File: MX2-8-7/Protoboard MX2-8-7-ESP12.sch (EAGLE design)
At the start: 140 parts, among them J1 DCJ0202

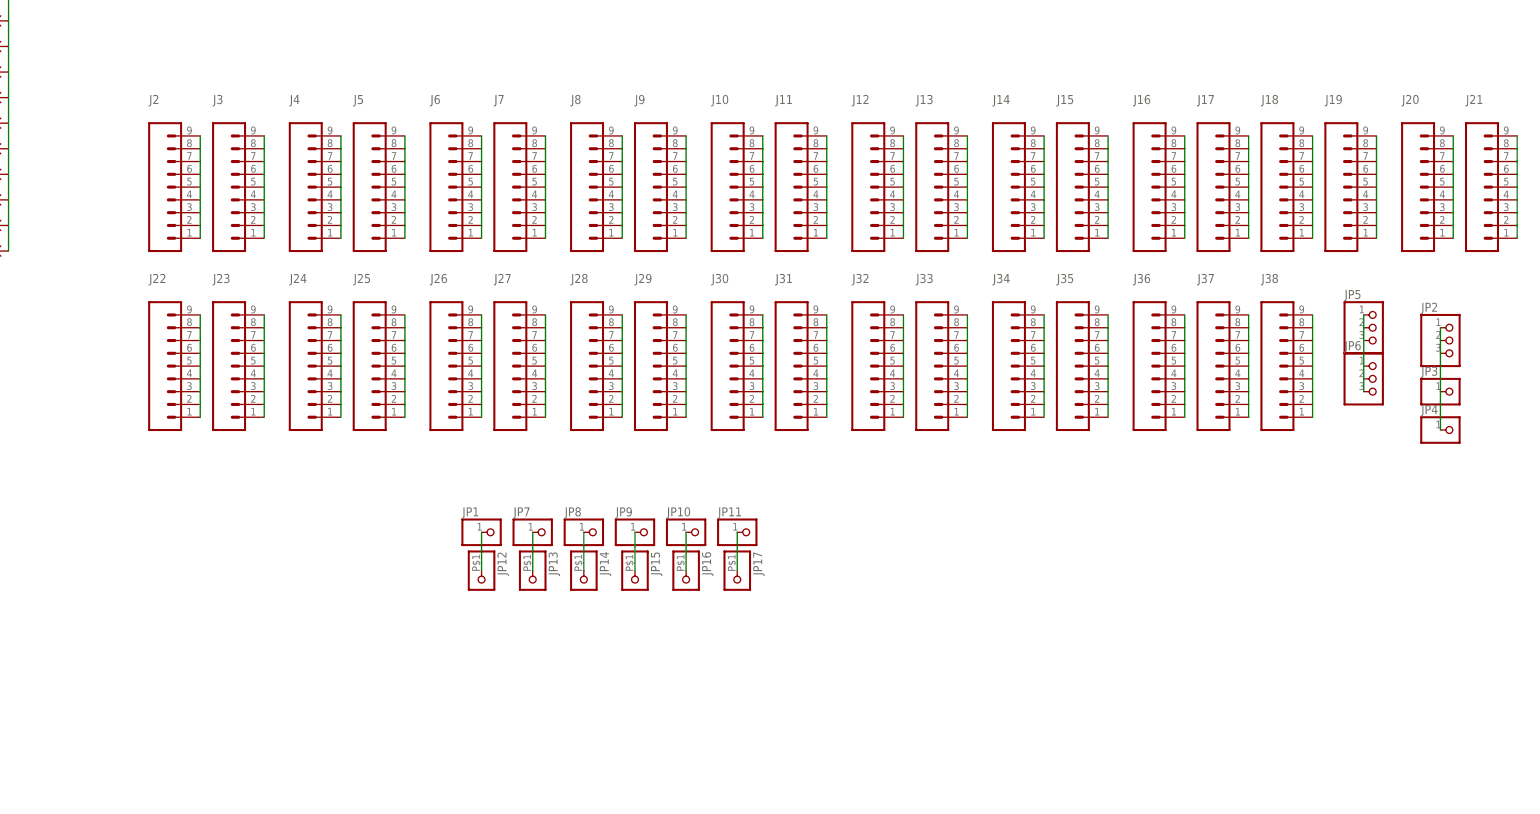
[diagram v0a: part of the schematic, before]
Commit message: Update to rev2
Updated to Pin headers instead of single wire pads
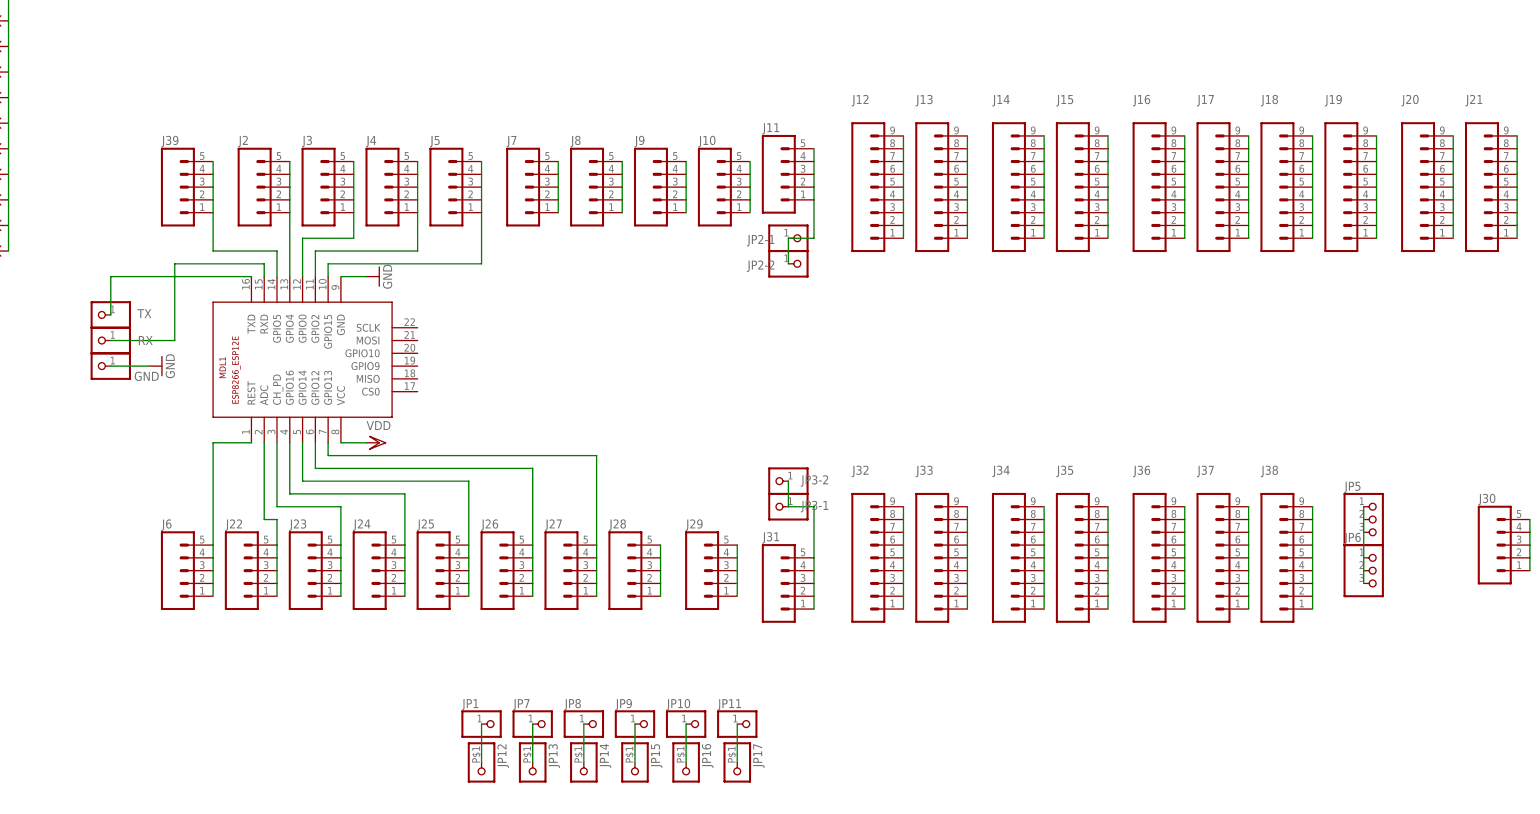
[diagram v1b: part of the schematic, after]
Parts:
- removed JP2: (no value), adafruit:PINHD-1X3CB
- removed JP3, JP4: (no value), adafruit:PINHD-1X1CB
- added GND, JP2-1, JP2-2, JP3-1, JP3-2, RX, TX: (no value), adafruit:PINHD-1X1CB
- added J39: (no value), SparkFun-Connectors:M05NO_SILK
- added MDL1: (no value), ESP8266-ESP12E:ESP8266-12EESP8266-ESP12E
- J10, J11, J2, J22, J23, J24, J25, J26, J27, J28, J29, J3, J30, J31, J4, J5, J6, J7, J8, J9: device SparkFun-Connectors:M09NO_SILK -> SparkFun-Connectors:M05NO_SILK
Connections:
- new net N$46: MDL1.RXD, RX.1
- new net N$47: MDL1.TXD, TX.1
- net GND: now also GND.1, MDL1.GND
- net N$1: now also J39.1, J39.2, J39.3, J39.4, J39.5, MDL1.GPIO5; no longer J2.1, J2.2, J2.3, J2.4, J2.5, J2.6, J2.7, J2.8, J2.9
- net N$10: no longer J10.6, J10.7, J10.8, J10.9
- net N$11: now also JP2-1.1, JP2-2.1; no longer J11.6, J11.7, J11.8, J11.9
- net N$22: now also J6.1, J6.2, J6.3, J6.4, J6.5, MDL1.REST; no longer J22.1, J22.2, J22.3, J22.4, J22.5, J22.6, J22.7, J22.8, J22.9
- net N$23: now also J22.1, J22.2, J22.3, J22.4, J22.5, MDL1.ADC; no longer J23.1, J23.2, J23.3, J23.4, J23.5, J23.6, J23.7, J23.8, J23.9
- net N$24: now also J23.1, J23.2, J23.3, J23.4, J23.5, MDL1.CH_PD; no longer J24.1, J24.2, J24.3, J24.4, J24.5, J24.6, J24.7, J24.8, J24.9
- net N$25: now also J24.1, J24.2, J24.3, J24.4, J24.5, MDL1.GPIO16; no longer J25.1, J25.2, J25.3, J25.4, J25.5, J25.6, J25.7, J25.8, J25.9
- net N$26: now also J25.1, J25.2, J25.3, J25.4, J25.5, MDL1.GPIO14; no longer J26.1, J26.2, J26.3, J26.4, J26.5, J26.6, J26.7, J26.8, J26.9
- net N$27: now also J26.1, J26.2, J26.3, J26.4, J26.5, MDL1.GPIO12; no longer J27.1, J27.2, J27.3, J27.4, J27.5, J27.6, J27.7, J27.8, J27.9
- net N$28: now also J27.1, J27.2, J27.3, J27.4, J27.5, MDL1.GPIO13; no longer J28.1, J28.2, J28.3, J28.4, J28.5, J28.6, J28.7, J28.8, J28.9
- net N$29: now also J28.1, J28.2, J28.3, J28.4, J28.5; no longer J29.1, J29.2, J29.3, J29.4, J29.5, J29.6, J29.7, J29.8, J29.9
- net N$3: now also J2.1, J2.2, J2.3, J2.4, J2.5, MDL1.GPIO4; no longer J3.1, J3.2, J3.3, J3.4, J3.5, J3.6, J3.7, J3.8, J3.9
- net N$30: now also J29.1, J29.2, J29.3, J29.4, J29.5; no longer J30.1, J30.2, J30.3, J30.4, J30.5, J30.6, J30.7, J30.8, J30.9
- net N$31: now also JP3-1.1, JP3-2.1; no longer J31.6, J31.7, J31.8, J31.9
- net N$4: now also J3.1, J3.2, J3.3, J3.4, J3.5, MDL1.GPIO0; no longer J4.1, J4.2, J4.3, J4.4, J4.5, J4.6, J4.7, J4.8, J4.9
- net N$41: now also J30.1, J30.2, J30.3, J30.4, J30.5; no longer JP2.1, JP2.2, JP2.3, JP3.1, JP4.1
- net N$5: now also J4.1, J4.2, J4.3, J4.4, J4.5, MDL1.GPIO2; no longer J5.1, J5.2, J5.3, J5.4, J5.5, J5.6, J5.7, J5.8, J5.9
- net N$6: now also J5.1, J5.2, J5.3, J5.4, J5.5, MDL1.GPIO15; no longer J6.1, J6.2, J6.3, J6.4, J6.5, J6.6, J6.7, J6.8, J6.9
- net N$7: no longer J7.6, J7.7, J7.8, J7.9
- net N$8: no longer J8.6, J8.7, J8.8, J8.9
- net N$9: no longer J9.6, J9.7, J9.8, J9.9
- net VDD: now also MDL1.VCC
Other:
- moved on the sheet: J32, J33, J34, J35, J36, J37, J38, JP1, JP10, JP11, JP12, JP13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

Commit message: Change usb connector
Change to correct usb connecter and moved esp8266 bit more onto the
board.
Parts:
- removed JP11: (no value), adafruit:PINHD-1X1CB
- removed JP17: (no value), adafruit:PINHD-1X1-BIGPOGO
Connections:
- removed net N$45: JP11.1, JP17.1
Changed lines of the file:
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@@
 <part name="JP9" library="adafruit" deviceset="PINHD-1X1" device="CB"/>
 <part name="JP10" library="adafruit" deviceset="PINHD-1X1" device="CB"/>
-<part name="JP11" library="adafruit" deviceset="PINHD-1X1" device="CB"/>
 <part name="JP12" library="adafruit" deviceset="PINHD-1X1" device="-BIGPOGO"/>
 <part name="JP13" library="adafruit" deviceset="PINHD-1X1" device="-BIGPOGO"/>
@@
 <part name="JP15" library="adafruit" deviceset="PINHD-1X1" device="-BIGPOGO"/>
 <part name="JP16" library="adafruit" deviceset="PINHD-1X1" device="-BIGPOGO"/>
-<part name="JP17" library="adafruit" deviceset="PINHD-1X1" device="-BIGPOGO"/>
 <part name="MDL1" library="ESP8266-ESP12E" deviceset="ESP8266-12E" device="ESP8266-ESP12E"/>
 <part name="J39" library="SparkFun-Connectors" deviceset="M05" device="NO_SILK"/>
@@
 <instance part="JP9" gate="G$1" x="162.56" y="-66.04"/>
 <instance part="JP10" gate="G$1" x="172.72" y="-66.04"/>
-<instance part="JP11" gate="G$1" x="182.88" y="-66.04"/>
 <instance part="JP12" gate="G$1" x="129.54" y="-76.2" rot="R270"/>
 <instance part="JP13" gate="G$1" x="139.7" y="-76.2" rot="R270"/>
@@
 <instance part="JP15" gate="G$1" x="160.02" y="-76.2" rot="R270"/>
 <instance part="JP16" gate="G$1" x="170.18" y="-76.2" rot="R270"/>
-<instance part="JP17" gate="G$1" x="180.34" y="-76.2" rot="R270"/>
 <instance part="MDL1" gate="G$1" x="91.44" y="12.7" rot="R90"/>
 <instance part="J39" gate="G$1" x="68.58" y="40.64"/>
@@
 </segment>
 </net>
-<net name="N$45" class="0">
-<segment>
-<pinref part="JP17" gate="G$1" pin="1"/>
-<pinref part="JP11" gate="G$1" pin="1"/>
-<wire x1="180.34" y1="-73.66" x2="180.34" y2="-66.04" width="0.1524" layer="91"/>
-</segment>
-</net>

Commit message: Update esp component and usb
test
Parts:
- removed J1: DCJ0202, con-jack:DCJ0202
- removed MDL1: (no value), ESP8266-ESP12E:ESP8266-12EESP8266-ESP12E
- added U2: (no value), SparkFun-PowerIC:MIC52053.3V
- added X1: ESP-12E, microbuilder:ESP-12E
- added X2: (no value), microbuilder:USB_MICRO_20329_V2
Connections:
- new net N$45: TX.1, X1.RXD
- net GND: now also U2.GND, X1.GND; no longer J1.2, J1.3, MDL1.GND
- net N$1: now also X1.GPIO5; no longer MDL1.GPIO5
- net N$22: now also X1.RESET; no longer MDL1.REST
- net N$23: now also X1.ADC; no longer MDL1.ADC
- net N$24: now also X1.CH_PD; no longer MDL1.CH_PD
- net N$25: now also X1.GPIO16; no longer MDL1.GPIO16
- net N$26: now also X1.GPIO14; no longer MDL1.GPIO14
- net N$27: now also X1.GPIO12; no longer MDL1.GPIO12
- net N$28: now also X1.GPIO13; no longer MDL1.GPIO13
- net N$3: now also X1.GPIO4; no longer MDL1.GPIO4
- net N$4: now also X1.GPIO0; no longer MDL1.GPIO0
- net N$46: now also X1.TXD; no longer MDL1.RXD
- net N$47: now also X2.GND; no longer MDL1.TXD, TX.1
- net N$5: now also X1.GPIO2; no longer MDL1.GPIO2
- net N$6: now also X1.GPIO15; no longer MDL1.GPIO15
- net VCC: now also U2.EN, U2.IN, X2.VBUS; no longer J1.1
- net VDD: now also U2.OUT, X1.VCC; no longer MDL1.VCC

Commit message: Routed
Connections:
- removed net N$7: J7.1, J7.2, J7.3, J7.4, J7.5
- removed net N$8: J8.1, J8.2, J8.3, J8.4, J8.5
- net N$45: now also J7.1, J7.2, J7.3, J7.4, J7.5
- net N$46: now also J8.1, J8.2, J8.3, J8.4, J8.5
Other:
- moved on the sheet: J7, J8
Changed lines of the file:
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@@
 <?xml version="1.0" encoding="utf-8"?>
 <!DOCTYPE eagle SYSTEM "eagle.dtd">
-<eagle version="7.7.0">
+<eagle version="7.6.0">
 <drawing>
 <settings>
@@
 <instance part="J26" gate="G$1" x="132.08" y="-35.56"/>
 <instance part="J27" gate="G$1" x="144.78" y="-35.56"/>
-<instance part="J7" gate="G$1" x="137.16" y="40.64"/>
-<instance part="J8" gate="G$1" x="149.86" y="40.64"/>
+<instance part="J7" gate="G$1" x="43.18" y="40.64"/>
+<instance part="J8" gate="G$1" x="55.88" y="40.64"/>
 <instance part="J9" gate="G$1" x="162.56" y="40.64"/>
 <instance part="J10" gate="G$1" x="175.26" y="40.64"/>
@@
 </segment>
 </net>
-<net name="N$7" class="0">
-<segment>
-<pinref part="J7" gate="G$1" pin="5"/>
-<pinref part="J7" gate="G$1" pin="4"/>
-<wire x1="144.78" y1="45.72" x2="144.78" y2="43.18" width="0.1524" layer="91"/>
-<pinref part="J7" gate="G$1" pin="3"/>
-<wire x1="144.78" y1="43.18" x2="144.78" y2="40.64" width="0.1524" layer="91"/>
-<pinref part="J7" gate="G$1" pin="2"/>
-<wire x1="144.78" y1="40.64" x2="144.78" y2="38.1" width="0.1524" layer="91"/>
-<pinref part="J7" gate="G$1" pin="1"/>
-<wire x1="144.78" y1="38.1" x2="144.78" y2="35.56" width="0.1524" layer="91"/>
-</segment>
-</net>
-<net name="N$8" class="0">
-<segment>
-<pinref part="J8" gate="G$1" pin="1"/>
-<pinref part="J8" gate="G$1" pin="2"/>
-<wire x1="157.48" y1="35.56" x2="157.48" y2="38.1" width="0.1524" layer="91"/>
-<pinref part="J8" gate="G$1" pin="3"/>
-<wire x1="157.48" y1="38.1" x2="157.48" y2="40.64" width="0.1524" layer="91"/>
-<pinref part="J8" gate="G$1" pin="4"/>
-<wire x1="157.48" y1="40.64" x2="157.48" y2="43.18" width="0.1524" layer="91"/>
-<pinref part="J8" gate="G$1" pin="5"/>
-<wire x1="157.48" y1="43.18" x2="157.48" y2="45.72" width="0.1524" layer="91"/>
-</segment>
-</net>
 <net name="N$9" class="0">
 <segment>
@@
 <wire x1="68.58" y1="10.16" x2="55.88" y2="10.16" width="0.1524" layer="91"/>
 <pinref part="X1" gate="G$1" pin="TXD"/>
+<pinref part="J8" gate="G$1" pin="1"/>
+<pinref part="J8" gate="G$1" pin="2"/>
+<wire x1="63.5" y1="35.56" x2="63.5" y2="38.1" width="0.1524" layer="91"/>
+<pinref part="J8" gate="G$1" pin="3"/>
+<wire x1="63.5" y1="38.1" x2="63.5" y2="40.64" width="0.1524" layer="91"/>
+<pinref part="J8" gate="G$1" pin="4"/>
+<wire x1="63.5" y1="40.64" x2="63.5" y2="43.18" width="0.1524" layer="91"/>
+<pinref part="J8" gate="G$1" pin="5"/>
+<wire x1="63.5" y1="43.18" x2="63.5" y2="45.72" width="0.1524" layer="91"/>
+<wire x1="68.58" y1="25.4" x2="63.5" y2="25.4" width="0.1524" layer="91"/>
+<wire x1="63.5" y1="25.4" x2="63.5" y2="35.56" width="0.1524" layer="91"/>
+<junction x="68.58" y="25.4"/>
 </segment>
 </net>
@@
 <wire x1="86.36" y1="25.4" x2="86.36" y2="26.924" width="0.1524" layer="91"/>
 <pinref part="TX" gate="G$1" pin="1"/>
-<wire x1="55.88" y1="26.924" x2="55.88" y2="15.24" width="0.1524" layer="91"/>
+<wire x1="55.88" y1="26.924" x2="55.88" y2="25.4" width="0.1524" layer="91"/>
+<wire x1="55.88" y1="25.4" x2="55.88" y2="15.24" width="0.1524" layer="91"/>
 <wire x1="86.36" y1="26.924" x2="55.88" y2="26.924" width="0.1524" layer="91"/>
-</segment>
-</net>
+<pinref part="J7" gate="G$1" pin="5"/>
+<pinref part="J7" gate="G$1" pin="4"/>
+<wire x1="50.8" y1="45.72" x2="50.8" y2="43.18" width="0.1524" layer="91"/>
+<pinref part="J7" gate="G$1" pin="3"/>
+<wire x1="50.8" y1="43.18" x2="50.8" y2="40.64" width="0.1524" layer="91"/>
+<pinref part="J7" gate="G$1" pin="2"/>
+<wire x1="50.8" y1="40.64" x2="50.8" y2="38.1" width="0.1524" layer="91"/>
+<pinref part="J7" gate="G$1" pin="1"/>
+<wire x1="50.8" y1="38.1" x2="50.8" y2="35.56" width="0.1524" layer="91"/>
+<wire x1="55.88" y1="25.4" x2="50.8" y2="25.4" width="0.1524" layer="91"/>
+<wire x1="50.8" y1="25.4" x2="50.8" y2="35.56" width="0.1524" layer="91"/>
+<junction x="55.88" y="25.4"/>
+</segment>
+</net>

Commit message: Revert "Routed"
This reverts commit 078e80659a45ef39a7709107a01737087c5908e1.
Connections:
- new net N$7: J7.1, J7.2, J7.3, J7.4, J7.5
- new net N$8: J8.1, J8.2, J8.3, J8.4, J8.5
- net N$45: no longer J7.1, J7.2, J7.3, J7.4, J7.5
- net N$46: no longer J8.1, J8.2, J8.3, J8.4, J8.5
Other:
- moved on the sheet: J7, J8
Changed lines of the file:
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@@
 <?xml version="1.0" encoding="utf-8"?>
 <!DOCTYPE eagle SYSTEM "eagle.dtd">
-<eagle version="7.6.0">
+<eagle version="7.7.0">
 <drawing>
 <settings>
@@
 <instance part="J26" gate="G$1" x="132.08" y="-35.56"/>
 <instance part="J27" gate="G$1" x="144.78" y="-35.56"/>
-<instance part="J7" gate="G$1" x="43.18" y="40.64"/>
-<instance part="J8" gate="G$1" x="55.88" y="40.64"/>
+<instance part="J7" gate="G$1" x="137.16" y="40.64"/>
+<instance part="J8" gate="G$1" x="149.86" y="40.64"/>
 <instance part="J9" gate="G$1" x="162.56" y="40.64"/>
 <instance part="J10" gate="G$1" x="175.26" y="40.64"/>
@@
 </segment>
 </net>
+<net name="N$7" class="0">
+<segment>
+<pinref part="J7" gate="G$1" pin="5"/>
+<pinref part="J7" gate="G$1" pin="4"/>
+<wire x1="144.78" y1="45.72" x2="144.78" y2="43.18" width="0.1524" layer="91"/>
+<pinref part="J7" gate="G$1" pin="3"/>
+<wire x1="144.78" y1="43.18" x2="144.78" y2="40.64" width="0.1524" layer="91"/>
+<pinref part="J7" gate="G$1" pin="2"/>
+<wire x1="144.78" y1="40.64" x2="144.78" y2="38.1" width="0.1524" layer="91"/>
+<pinref part="J7" gate="G$1" pin="1"/>
+<wire x1="144.78" y1="38.1" x2="144.78" y2="35.56" width="0.1524" layer="91"/>
+</segment>
+</net>
+<net name="N$8" class="0">
+<segment>
+<pinref part="J8" gate="G$1" pin="1"/>
+<pinref part="J8" gate="G$1" pin="2"/>
+<wire x1="157.48" y1="35.56" x2="157.48" y2="38.1" width="0.1524" layer="91"/>
+<pinref part="J8" gate="G$1" pin="3"/>
+<wire x1="157.48" y1="38.1" x2="157.48" y2="40.64" width="0.1524" layer="91"/>
+<pinref part="J8" gate="G$1" pin="4"/>
+<wire x1="157.48" y1="40.64" x2="157.48" y2="43.18" width="0.1524" layer="91"/>
+<pinref part="J8" gate="G$1" pin="5"/>
+<wire x1="157.48" y1="43.18" x2="157.48" y2="45.72" width="0.1524" layer="91"/>
+</segment>
+</net>
 <net name="N$9" class="0">
 <segment>
@@
 <wire x1="68.58" y1="10.16" x2="55.88" y2="10.16" width="0.1524" layer="91"/>
 <pinref part="X1" gate="G$1" pin="TXD"/>
-<pinref part="J8" gate="G$1" pin="1"/>
-<pinref part="J8" gate="G$1" pin="2"/>
-<wire x1="63.5" y1="35.56" x2="63.5" y2="38.1" width="0.1524" layer="91"/>
-<pinref part="J8" gate="G$1" pin="3"/>
-<wire x1="63.5" y1="38.1" x2="63.5" y2="40.64" width="0.1524" layer="91"/>
-<pinref part="J8" gate="G$1" pin="4"/>
-<wire x1="63.5" y1="40.64" x2="63.5" y2="43.18" width="0.1524" layer="91"/>
-<pinref part="J8" gate="G$1" pin="5"/>
-<wire x1="63.5" y1="43.18" x2="63.5" y2="45.72" width="0.1524" layer="91"/>
-<wire x1="68.58" y1="25.4" x2="63.5" y2="25.4" width="0.1524" layer="91"/>
-<wire x1="63.5" y1="25.4" x2="63.5" y2="35.56" width="0.1524" layer="91"/>
-<junction x="68.58" y="25.4"/>
 </segment>
 </net>
@@
 <wire x1="86.36" y1="25.4" x2="86.36" y2="26.924" width="0.1524" layer="91"/>
 <pinref part="TX" gate="G$1" pin="1"/>
-<wire x1="55.88" y1="26.924" x2="55.88" y2="25.4" width="0.1524" layer="91"/>
-<wire x1="55.88" y1="25.4" x2="55.88" y2="15.24" width="0.1524" layer="91"/>
+<wire x1="55.88" y1="26.924" x2="55.88" y2="15.24" width="0.1524" layer="91"/>
 <wire x1="86.36" y1="26.924" x2="55.88" y2="26.924" width="0.1524" layer="91"/>
-<pinref part="J7" gate="G$1" pin="5"/>
-<pinref part="J7" gate="G$1" pin="4"/>
-<wire x1="50.8" y1="45.72" x2="50.8" y2="43.18" width="0.1524" layer="91"/>
-<pinref part="J7" gate="G$1" pin="3"/>
-<wire x1="50.8" y1="43.18" x2="50.8" y2="40.64" width="0.1524" layer="91"/>
-<pinref part="J7" gate="G$1" pin="2"/>
-<wire x1="50.8" y1="40.64" x2="50.8" y2="38.1" width="0.1524" layer="91"/>
-<pinref part="J7" gate="G$1" pin="1"/>
-<wire x1="50.8" y1="38.1" x2="50.8" y2="35.56" width="0.1524" layer="91"/>
-<wire x1="55.88" y1="25.4" x2="50.8" y2="25.4" width="0.1524" layer="91"/>
-<wire x1="50.8" y1="25.4" x2="50.8" y2="35.56" width="0.1524" layer="91"/>
-<junction x="55.88" y="25.4"/>
-</segment>
-</net>
+</segment>
+</net>
